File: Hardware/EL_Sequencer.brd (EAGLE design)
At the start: 57.1 x 82.5 mm, 107 parts, among them J1 Battery, J2 DC-OUTPUT, J3 AC-INPUT, U1 LM317, U10 Z0103MN, U11 Z0103MN, U12 Z0103MN, U13 MOC3063S, U14 MOC3063S, U15 MOC3063S, U16 MOC3063S, U17 Z0103MN, U18 Z0103MN, U19 Z0103MN, U2 MIC5219-3.3, U20 Z0103MN, U3 ATMEGA328P, U4-DNP XBEE HEADER, U5 MOC3063S, U6 MOC3063S, U7 MOC3063S, U8 MOC3063S, U9 Z0103MN, Y1 8MHz

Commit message: changed fiducials
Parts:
- removed U$3, U$4: FIDUCIALUFIDUCIAL, SparkFun-Aesthetics:MICRO-FIDUCIAL
- added FID1, FID2: FIDUCIAL1X2, SparkFun-Aesthetics:FIDUCIAL-1X2

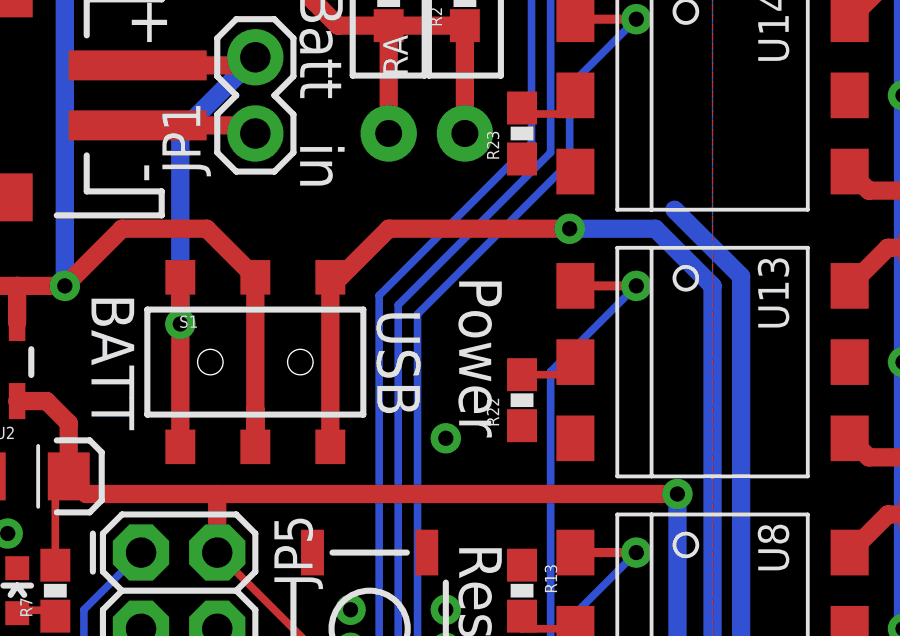
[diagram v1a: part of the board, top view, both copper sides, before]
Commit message: Adding Schottky diode to 5VUSB line for feedback protection
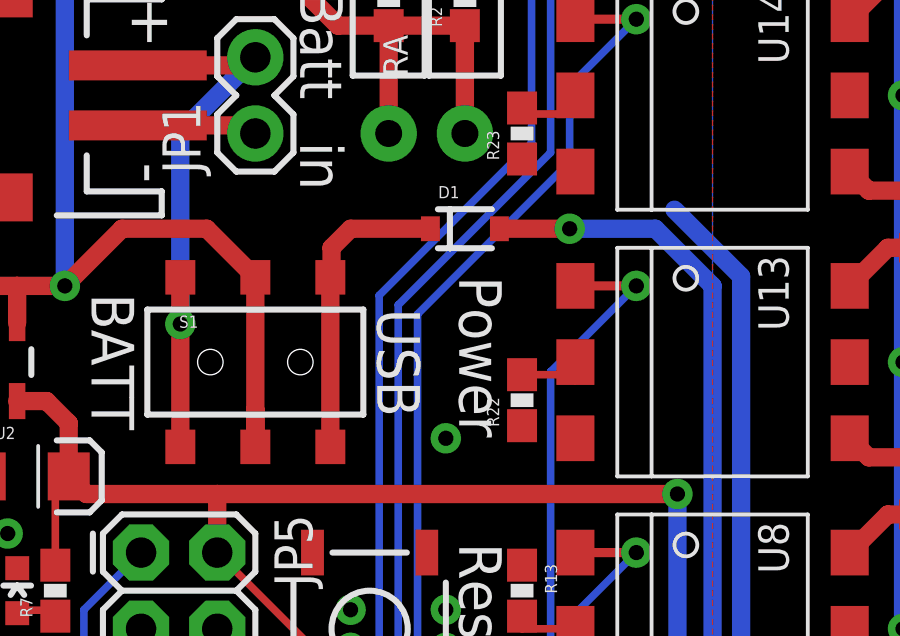
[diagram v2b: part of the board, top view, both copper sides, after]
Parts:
- added D1: PMEG4005EJ, SparkFun-DiscreteSemi:SOD-323
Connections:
- new net DIO_VBUS: D1.C, S1.3, S1.6
- net 5VUSB: now also D1.A; no longer S1.3, S1.6
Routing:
- net 5VUSB: track 77.9 -> 65.8 mm
- net DIO_VBUS: track 0.00 -> 10.2 mm

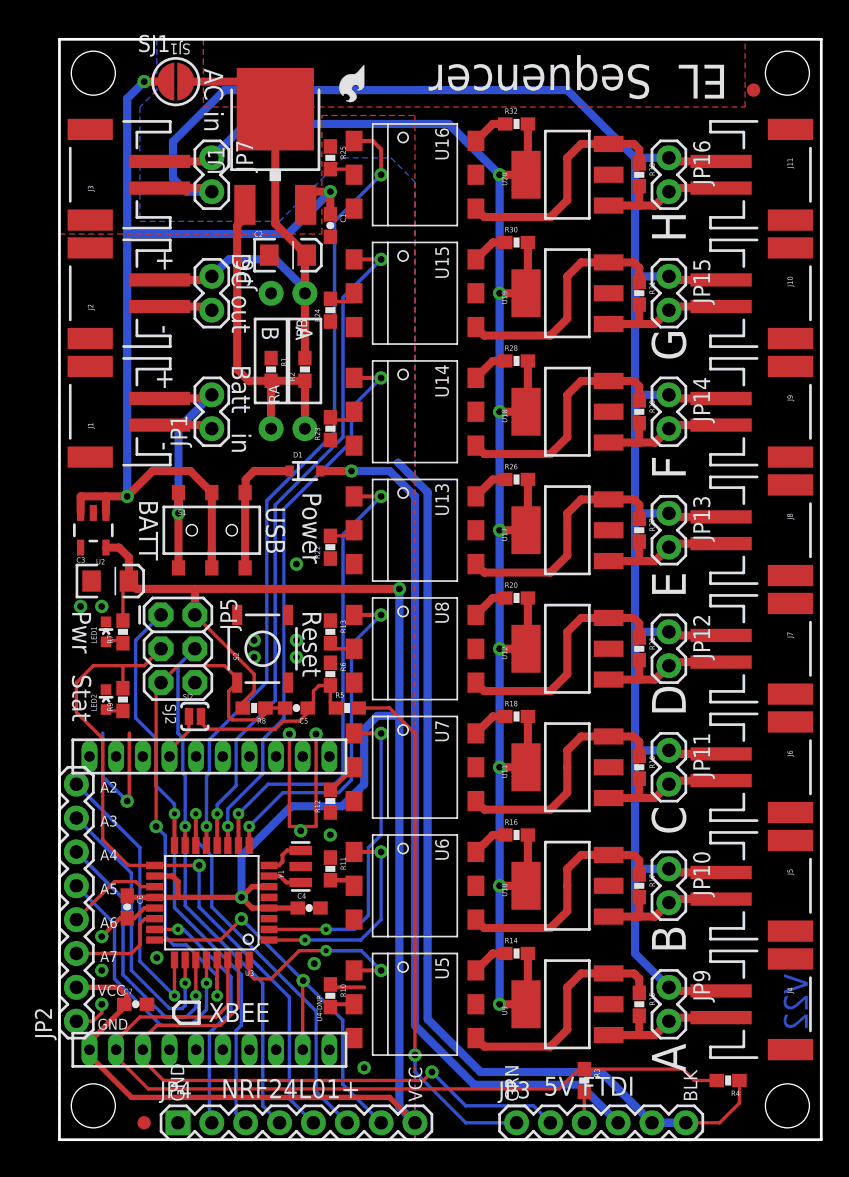
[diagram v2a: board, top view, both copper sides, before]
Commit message: Adding in switch for FTDI/XBee selection
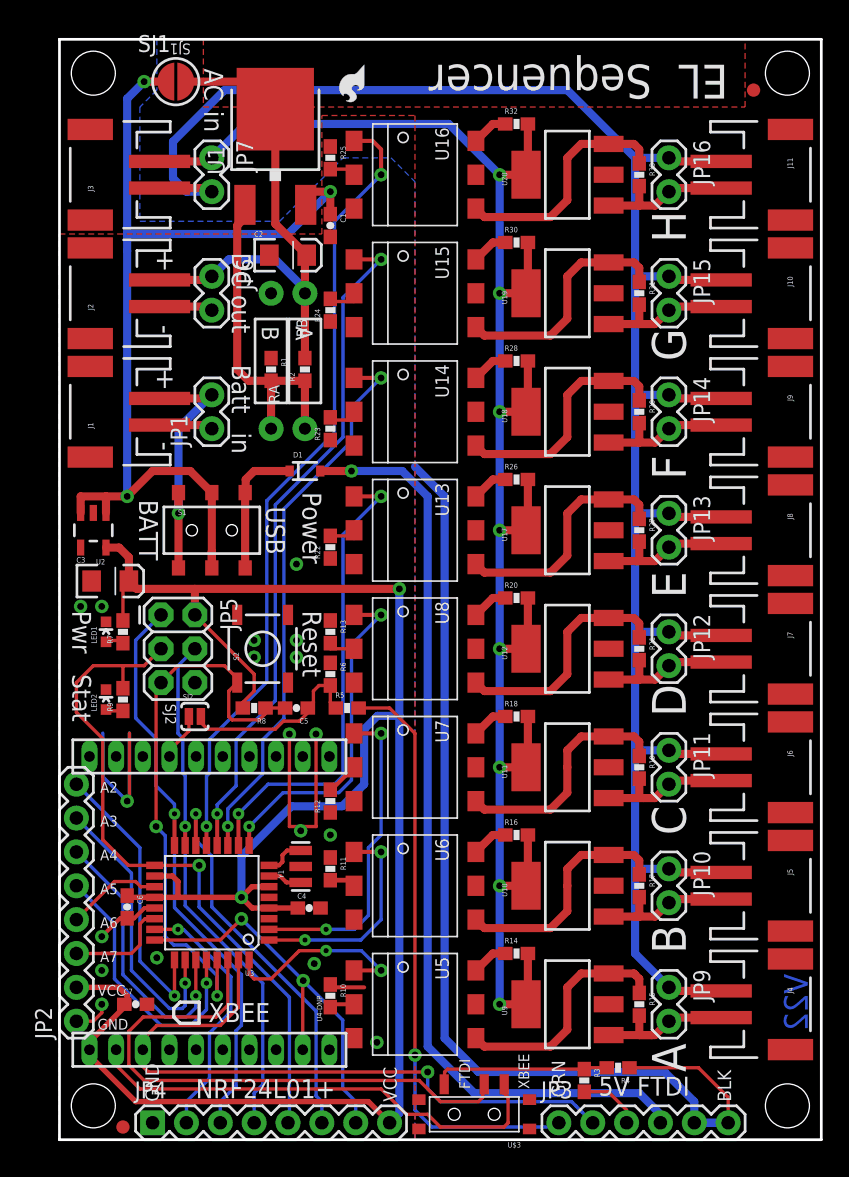
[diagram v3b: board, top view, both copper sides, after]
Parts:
- added U$3: SWITCH_SPDT, SparkFun-Electromechanical:KPS-1290
- moved R4 8.31 mm to (41.9, 5.40)
- moved JP3 3.18 mm to (37.5, 1.27)
- moved JP4 1.91 mm to (6.99, 1.27)
- moved FID1 1.62 mm to (4.76, 0.95)
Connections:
- new net RXI_FTDI: R3.1, R4.2, U$3.O
- new net RXI_XBEE: U$3.S, U4-DNP.2
- net RXI: now also U$3.P; no longer R3.1, R4.2, U4-DNP.2
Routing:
- net RXI_XBEE: track 0.00 -> 35.6 mm
- net RXI: track 61.1 -> 43.0 mm
- net RXI_FTDI: track 0.00 -> 13.2 mm
- net GND: track 122.3 -> 129.5 mm
- net FTDI_DTR: track 39.6 -> 44.7 mm
- net 5VUSB: track 65.8 -> 70.3 mm
- net TXO: track 46.3 -> 50.0 mm
- net FTDI_RXI: track 2.33 -> 4.70 mm
- net VCC: track 156.3 -> 154.2 mm
- net CSN: track 30.3 -> 29.5 mm
- net CE/SLEEP: track 32.0 -> 31.2 mm
- net SCK: track 52.6 -> 51.9 mm
- net IRQ: track 18.9 -> 19.5 mm
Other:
- board text added: "FTDI"

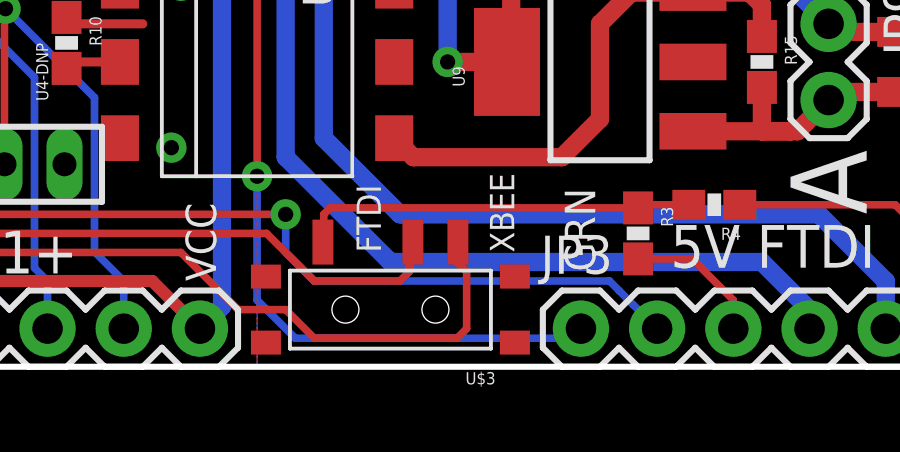
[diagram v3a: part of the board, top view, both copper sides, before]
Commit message: Very minor adjustments
Fixed misaligned text in bplace (probably old)
Minor routing tweaks to switch pads (centered trc)
Renamed switch from U$3 to S3 (lib problem)
Reduced R9 to 470 to brighten green LED2
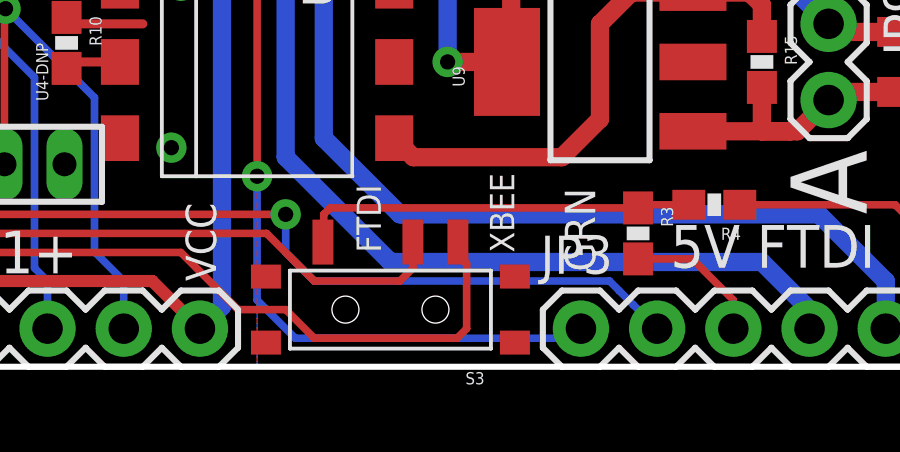
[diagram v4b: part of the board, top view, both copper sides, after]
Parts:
- R9: value 1K -> 470
- renumbered U$3 to S3
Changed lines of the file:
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@@
 <?xml version="1.0" encoding="utf-8"?>
 <!DOCTYPE eagle SYSTEM "eagle.dtd">
-<eagle version="6.5.0">
+<eagle version="6.4">
 <drawing>
 <settings>
@@
 <grid distance="0.0125" unitdist="inch" unit="inch" style="lines" multiple="2" display="yes" altdistance="0.005" altunitdist="inch" altunit="inch"/>
 <layers>
-<layer number="1" name="Top" color="4" fill="1" visible="yes" active="yes"/>
+<layer number="1" name="Top" color="4" fill="1" visible="no" active="yes"/>
 <layer number="2" name="Route2" color="1" fill="3" visible="no" active="no"/>
 <layer number="3" name="Route3" color="4" fill="3" visible="no" active="no"/>
@@
 <layer number="14" name="Route14" color="1" fill="6" visible="no" active="no"/>
 <layer number="15" name="Route15" color="4" fill="6" visible="no" active="no"/>
-<layer number="16" name="Bottom" color="1" fill="1" visible="yes" active="yes"/>
+<layer number="16" name="Bottom" color="1" fill="1" visible="no" active="yes"/>
 <layer number="17" name="Pads" color="2" fill="1" visible="yes" active="yes"/>
 <layer number="18" name="Vias" color="2" fill="1" visible="yes" active="yes"/>
 <layer number="19" name="Unrouted" color="6" fill="1" visible="yes" active="yes"/>
-<layer number="20" name="Dimension" color="15" fill="1" visible="yes" active="yes"/>
+<layer number="20" name="Dimension" color="15" fill="1" visible="no" active="yes"/>
 <layer number="21" name="tPlace" color="16" fill="1" visible="yes" active="yes"/>
-<layer number="22" name="bPlace" color="14" fill="1" visible="yes" active="yes"/>
-<layer number="23" name="tOrigins" color="15" fill="1" visible="yes" active="yes"/>
-<layer number="24" name="bOrigins" color="15" fill="1" visible="yes" active="yes"/>
+<layer number="22" name="bPlace" color="14" fill="1" visible="no" active="yes"/>
+<layer number="23" name="tOrigins" color="15" fill="1" visible="no" active="yes"/>
+<layer number="24" name="bOrigins" color="15" fill="1" visible="no" active="yes"/>
 <layer number="25" name="tNames" color="7" fill="1" visible="no" active="yes"/>
 <layer number="26" name="bNames" color="7" fill="1" visible="no" active="yes"/>
 <layer number="27" name="tValues" color="7" fill="1" visible="no" active="yes"/>
 <layer number="28" name="bValues" color="7" fill="1" visible="no" active="yes"/>
-<layer number="29" name="tStop" color="7" fill="3" visible="no" active="yes"/>
+<layer number="29" name="tStop" color="7" fill="3" visible="yes" active="yes"/>
 <layer number="30" name="bStop" color="7" fill="6" visible="no" active="yes"/>
 <layer number="31" name="tCream" color="7" fill="4" visible="no" active="yes"/>
@@
 <layer number="37" name="tTest" color="7" fill="1" visible="no" active="yes"/>
 <layer number="38" name="bTest" color="7" fill="1" visible="no" active="yes"/>
-<layer number="39" name="tKeepout" color="4" fill="11" visible="no" active="yes"/>
+<layer number="39" name="tKeepout" color="4" fill="11" visible="yes" active="yes"/>
 <layer number="40" name="bKeepout" color="1" fill="11" visible="no" active="yes"/>
 <layer number="41" name="tRestrict" color="4" fill="10" visible="no" active="yes"/>
 <layer number="42" name="bRestrict" color="1" fill="10" visible="no" active="yes"/>
 <layer number="43" name="vRestrict" color="2" fill="10" visible="no" active="yes"/>
-<layer number="44" name="Drills" color="7" fill="1" visible="no" active="yes"/>
+<layer number="44" name="Drills" color="7" fill="1" visible="yes" active="yes"/>
 <layer number="45" name="Holes" color="7" fill="1" visible="yes" active="yes"/>
 <layer number="46" name="Milling" color="3" fill="1" visible="no" active="yes"/>
 <layer number="47" name="Measures" color="7" fill="1" visible="no" active="yes"/>
 <layer number="48" name="Document" color="7" fill="1" visible="no" active="yes"/>
-<layer number="49" name="Reference" color="7" fill="1" visible="yes" active="yes"/>
+<layer number="49" name="Reference" color="7" fill="1" visible="no" active="yes"/>
 <layer number="50" name="dxf" color="7" fill="1" visible="no" active="yes"/>
-<layer number="51" name="tDocu" color="6" fill="1" visible="yes" active="yes"/>
+<layer number="51" name="tDocu" color="6" fill="1" visible="no" active="yes"/>
 <layer number="52" name="bDocu" color="7" fill="1" visible="no" active="yes"/>
 <layer number="53" name="tGND_GNDA" color="7" fill="9" visible="no" active="no"/>
@@
 <text x="3.048" y="13.335" size="0.8128" layer="21" font="vector" ratio="15">A7</text>
 <text x="50.8" y="6.0325" size="1.27" layer="22" font="vector" ratio="15" rot="SMR270">GND</text>
-<text x="47.9425" y="6.0325" size="1.27" layer="22" font="vector" ratio="15" rot="SMR270">GND</text>
+<text x="48.26" y="6.0325" size="1.27" layer="22" font="vector" ratio="15" rot="SMR270">GND</text>
 <text x="43.18" y="5.715" size="1.27" layer="22" font="vector" ratio="15" rot="SMR270">RXI</text>
 <text x="40.64" y="6.0325" size="1.27" layer="22" font="vector" ratio="15" rot="SMR270">TXO</text>
 <text x="38.1" y="6.0325" size="1.27" layer="22" font="vector" ratio="15" rot="SMR270">DTR</text>
-<text x="45.4025" y="4.92125" size="1.27" layer="22" font="vector" ratio="15" rot="SMR270">5V</text>
+<text x="45.72" y="4.92125" size="1.27" layer="22" font="vector" ratio="15" rot="SMR270">5V</text>
 <text x="2.8575" y="8.255" size="0.8128" layer="21" font="vector" ratio="15">GND</text>
 <text x="2.8575" y="10.795" size="0.8128" layer="21" font="vector" ratio="15">VCC</text>
@@
 <text x="15.24" y="4.92125" size="1.27" layer="22" font="vector" ratio="15" rot="SMR270">MO</text>
 <text x="17.78" y="5.715" size="1.27" layer="22" font="vector" ratio="15" rot="SMR270">SCK</text>
-<text x="20.0025" y="6.0325" size="1.27" layer="22" font="vector" ratio="15" rot="SMR270">CSN</text>
+<text x="20.32" y="5.715" size="1.27" layer="22" font="vector" ratio="15" rot="SMR270">CSN</text>
 <text x="22.86" y="4.92125" size="1.27" layer="22" font="vector" ratio="15" rot="SMR270">CE</text>
 <text x="25.4" y="6.0325" size="1.27" layer="22" font="vector" ratio="15" rot="SMR270">VCC</text>
@@
 <element name="U3" library="SparkFun" package="TQFP32-08" value="ATMEGA328P" x="11.43" y="17.78" rot="R180"/>
 <element name="LED2" library="SparkFun" package="LED-0603" value="Status" x="3.4925" y="33.02"/>
-<element name="R9" library="SparkFun-Resistors" package="0603-RES" value="1K" x="4.7625" y="33.02" rot="R90">
+<element name="R9" library="SparkFun-Resistors" package="0603-RES" value="470" x="4.7625" y="33.02" rot="R90">
 <attribute name="PROD_ID" value="RES-07856" x="4.7625" y="33.02" size="1.778" layer="27" rot="R90" display="off"/>
 <attribute name="VALUE" value="1K" x="4.7625" y="33.02" size="1.778" layer="27" rot="R90" display="off"/>
@@
 <attribute name="PROD_ID" value="DIO-10955" x="18.415" y="50.165" size="1.778" layer="27" font="vector" ratio="15" display="off"/>
 </element>
-<element name="U$3" library="SparkFun-Electromechanical" package="KPS-1290" value="SWITCH_SPDT" x="31.115" y="1.905">
+<element name="S3" library="SparkFun-Electromechanical" package="KPS-1290" value="SWITCH_SPDT" x="31.115" y="1.905">
 <attribute name="PROD_ID" value="SWCH-10651" x="31.115" y="1.905" size="1.778" layer="27" font="vector" ratio="15" display="off"/>
 </element>
@@
 <contactref element="U3" pad="30"/>
 <wire x1="12.63" y1="13.4874" x2="12.63" y2="10.09" width="0.254" layer="1"/>
-<contactref element="U$3" pad="P"/>
+<contactref element="S3" pad="P"/>
 <wire x1="12.63" y1="10.09" x2="11.7475" y2="9.2075" width="0.254" layer="1"/>
 <wire x1="26.9875" y1="4.445" x2="28.575" y2="2.8575" width="0.254" layer="1"/>
 <wire x1="28.575" y1="2.8575" x2="31.4325" y2="2.8575" width="0.254" layer="1"/>
-<wire x1="31.4325" y1="2.8575" x2="31.75" y2="3.175" width="0.254" layer="1"/>
-<wire x1="31.75" y1="3.175" x2="31.75" y2="4.04" width="0.254" layer="1"/>
-<wire x1="31.75" y1="4.04" x2="31.865" y2="4.155" width="0.254" layer="1"/>
 <wire x1="6.2865" y1="9.2075" x2="11.7475" y2="9.2075" width="0.254" layer="1"/>
 <wire x1="6.2865" y1="9.2075" x2="5.207" y2="8.128" width="0.254" layer="1"/>
@@
 <wire x1="5.207" y1="5.588" x2="6.35" y2="4.445" width="0.254" layer="1"/>
 <wire x1="6.35" y1="4.445" x2="26.9875" y2="4.445" width="0.254" layer="1"/>
+<wire x1="31.865" y1="4.155" x2="31.865" y2="3.29" width="0.254" layer="1"/>
+<wire x1="31.865" y1="3.29" x2="31.4325" y2="2.8575" width="0.254" layer="1"/>
 </signal>
 <signal name="TXO">
@@
 </signal>
 <signal name="RXI_FTDI">
-<contactref element="U$3" pad="O"/>
+<contactref element="S3" pad="O"/>
 <contactref element="R3" pad="1"/>
 <contactref element="R4" pad="2"/>
@@
 </signal>
 <signal name="RXI_XBEE">
-<contactref element="U$3" pad="S"/>
+<contactref element="S3" pad="S"/>
 <contactref element="U4-DNP" pad="2"/>
 <wire x1="4.25" y1="6.75" x2="4.25" y2="5.5925" width="0.254" layer="1"/>
@@
 <wire x1="28.575" y1="0.9525" x2="33.3375" y2="0.9525" width="0.254" layer="1"/>
 <wire x1="33.3375" y1="0.9525" x2="33.655" y2="1.27" width="0.254" layer="1"/>
-<wire x1="33.655" y1="1.27" x2="33.655" y2="3.175" width="0.254" layer="1"/>
-<wire x1="33.655" y1="3.175" x2="33.3375" y2="3.4925" width="0.254" layer="1"/>
-<wire x1="33.3375" y1="3.4925" x2="33.3375" y2="4.1275" width="0.254" layer="1"/>
+<wire x1="33.655" y1="1.27" x2="33.655" y2="3.429" width="0.254" layer="1"/>
 <wire x1="33.3375" y1="4.1275" x2="33.365" y2="4.155" width="0.254" layer="1"/>
 <wire x1="4.25" y1="5.5925" x2="6.0325" y2="3.81" width="0.254" layer="1"/>
 <wire x1="6.0325" y1="3.81" x2="24.13" y2="3.81" width="0.254" layer="1"/>
 <wire x1="24.13" y1="3.81" x2="26.035" y2="1.905" width="0.254" layer="1"/>
+<wire x1="33.365" y1="4.155" x2="33.365" y2="3.719" width="0.254" layer="1"/>
+<wire x1="33.365" y1="3.719" x2="33.655" y2="3.429" width="0.254" layer="1"/>
 </signal>
 </signals>
-<errors>
-</errors>
 </board>
 </drawing>
